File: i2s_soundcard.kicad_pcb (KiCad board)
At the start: 4 copper layers, 83.1 x 38.1 mm, 23 parts, among them J1 Conn_01x08, J2 Conn_01x06, J3 Conn_01x04, J4 Conn_01x11, J5 Conn_01x03, U1 TLV320AIC3104IRHBT, U2 TPA2006D1DRBR, U3 TPA2006D1DRBR, U6 TLV7111830DSER, U7 TPD4E02B04DQAR, U8 TPD4E02B04DQAR

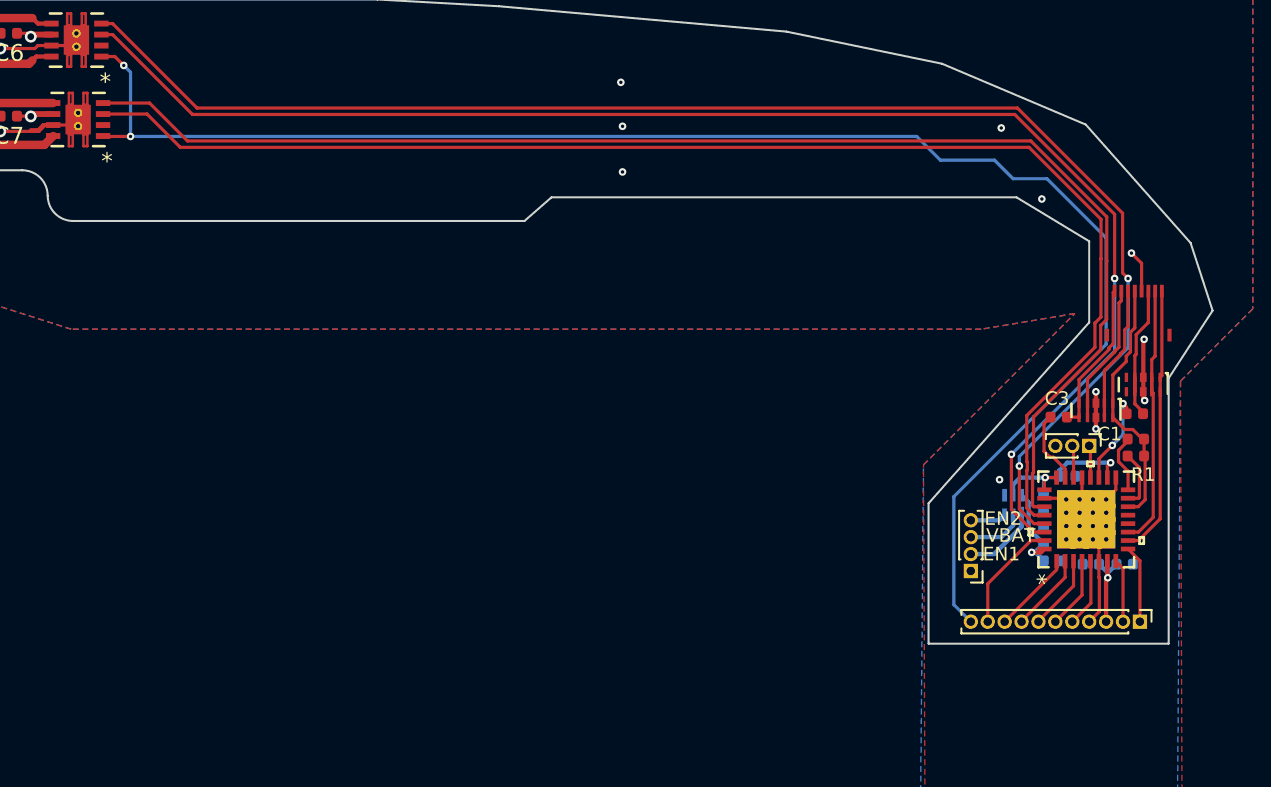
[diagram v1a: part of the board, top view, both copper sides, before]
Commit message: Change C2/C3 to 1206, adjust board to make that fit. Add courtyard to ESD protection diodes
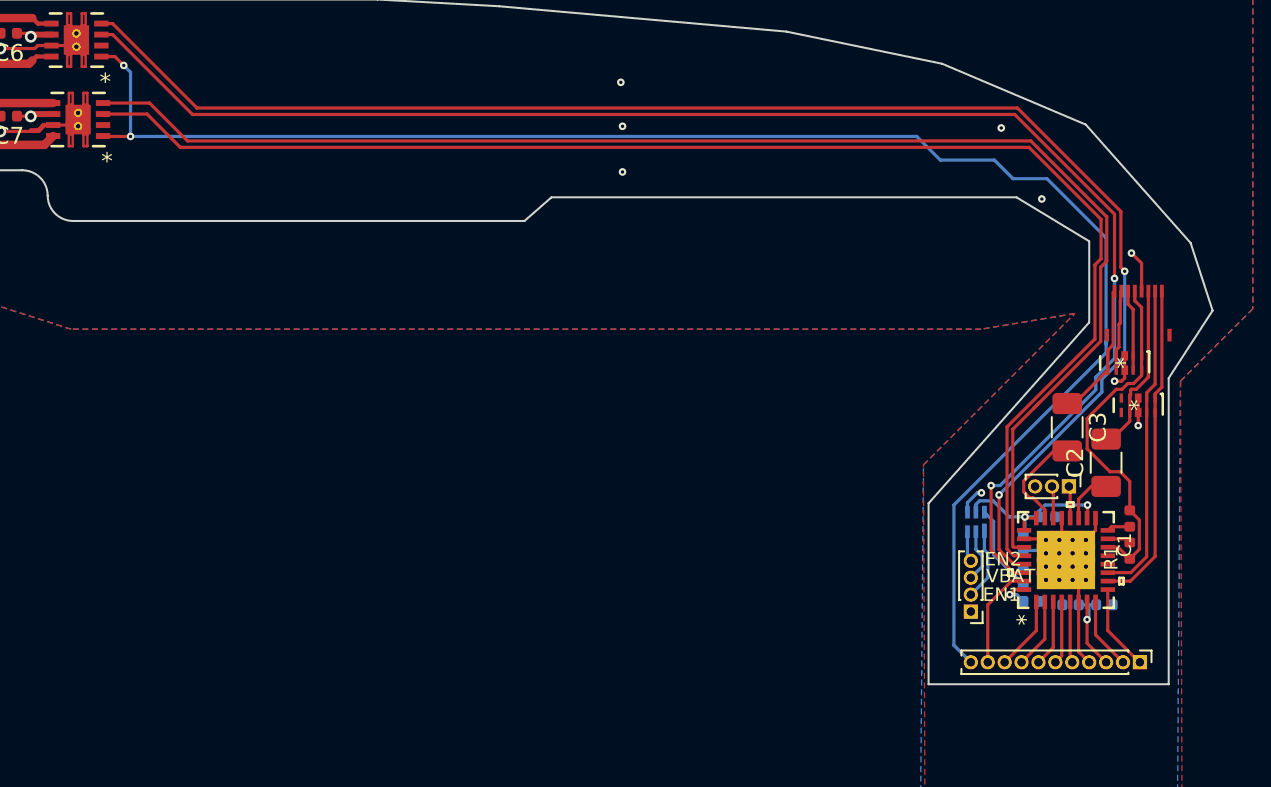
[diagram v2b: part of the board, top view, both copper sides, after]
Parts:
- C1: value C -> 100nF
- C2, C3: value C -> 220uF; footprint Capacitor_SMD:C_0402_1005Metric -> Capacitor_SMD:C_1206_3216Metric
- U7, U8: value TPD4E02B04DQAR -> DQA0010A
- moved R1 5.61 mm to (166.0, 90.9), turned to 90 degrees
- moved C1 4.71 mm to (166.0, 89.0), turned to 90 degrees
- moved C2 3.36 mm to (164.6, 85.7), turned to 90 degrees
- moved U8 3.28 mm to (165.7, 79.8)
- moved C4 2.68 mm to (159.7, 92.4)
- moved C5 2.68 mm to (159.7, 90.4)
- moved C8 2.68 mm to (160.2, 93.9)
- moved C9 2.68 mm to (161.1, 88.9)
- moved U1 2.68 mm to (162.2, 91.5)
- moved C10 2.68 mm to (162.5, 94.1)
- moved C11 2.68 mm to (164.5, 94.1)
- moved J5 2.68 mm to (162.4, 87.1)
- moved U6 2.42 mm to (156.9, 89.2)
- moved J3 2.40 mm to (156.6, 94.5)
- moved J4 2.40 mm to (166.6, 97.5)
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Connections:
- U1 pad 12: (no net) -> Net-(U1-Pad12)
- U1 pad 13: (no net) -> Net-(U1-Pad13)
- U2 pad 2: (no net) -> Net-(U2-Pad2)
- U3 pad 2: (no net) -> Net-(U3-Pad2)
- U7 pad 5: (no net) -> Net-(U7-Pad5)
- U7 pad 6: (no net) -> Net-(U7-Pad6)
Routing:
- net GND: track 36.5 -> 29.8 mm, vias 15 -> 13
- net /SLEEVE: track 15.2 -> 21.2 mm
- net /DETECT?: track 8.30 -> 4.80 mm
- net /spkr_amp_left/LINEIN+: track 81.8 -> 85.1 mm
- net /INTMIC_P: track 15.9 -> 19.3 mm
- net /RING2_AGAIN: track 8.05 -> 4.80 mm
- net /spkr_amp_right/LINEIN-: track 86.8 -> 90.0 mm
- net /spkr_amp_left/LINEIN-: track 81.7 -> 84.6 mm
- net /spkr_amp_right/LINEIN+: track 87.1 -> 89.9 mm
- net Net-(C2-Pad1): track 5.75 -> 3.06 mm, vias 2 -> 0
- net /~SHUTDOWN: track 94.5 -> 97.1 mm
- net /INTMIC_N: track 16.2 -> 18.6 mm
- net Net-(C1-Pad1): track 3.46 -> 1.39 mm
- net Net-(R1-Pad2): track 3.43 -> 1.39 mm
- net Net-(C3-Pad2): track 4.37 -> 6.13 mm
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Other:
- board size 83.1 x 38.1 mm -> 83.1 x 40.5 mm

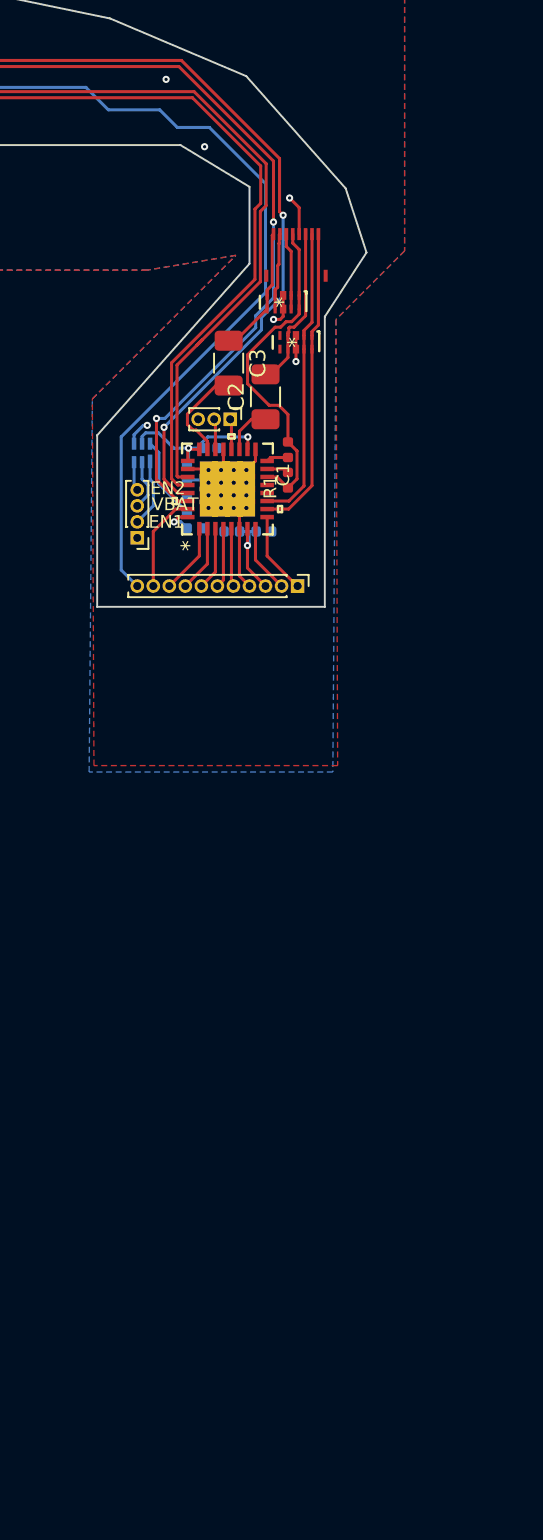
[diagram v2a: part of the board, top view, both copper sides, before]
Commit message: lay out new version with AIC3206 codec
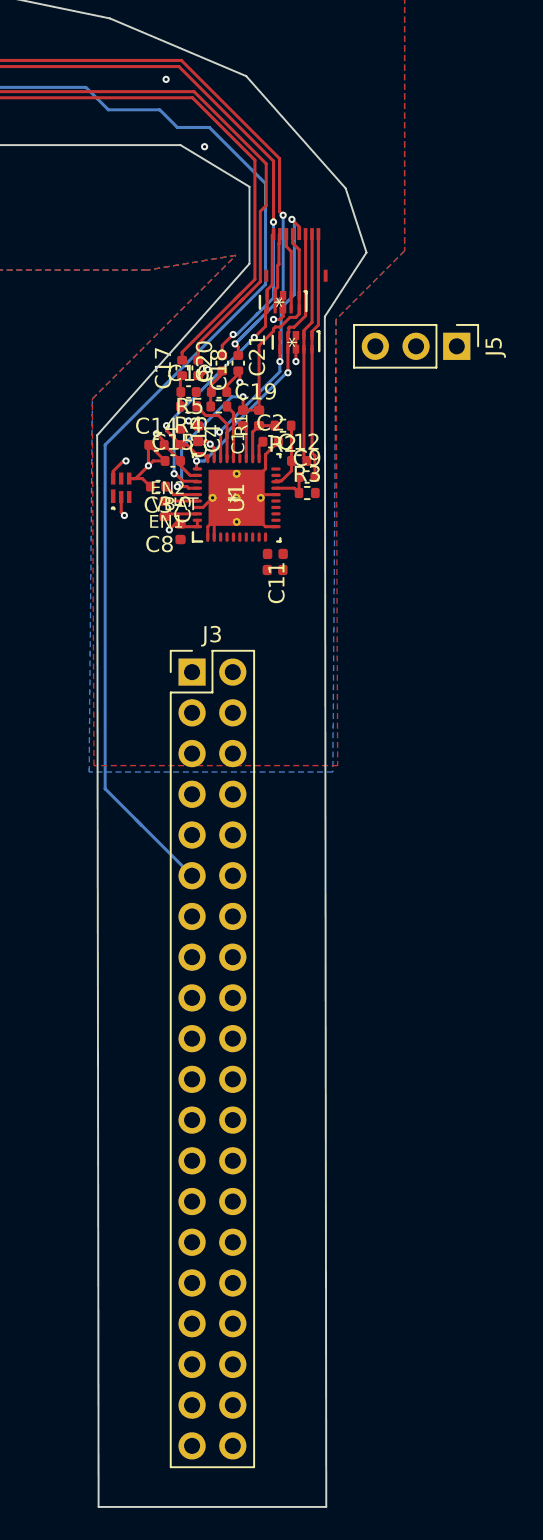
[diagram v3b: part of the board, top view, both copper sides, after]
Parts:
- removed J4: Conn_01x11, Connector_PinHeader_1.00mm:PinHeader_1x11_P1.00mm_Vertical
- added C12: 0.1u, Capacitor_SMD:C_0402_1005Metric, F.Cu at (166.7, 89.7)
- added C13: 10uF, Capacitor_SMD:C_0402_1005Metric, F.Cu at (159.3, 88.2)
- added C14: 10uF, Capacitor_SMD:C_0402_1005Metric, F.Cu at (157.8, 88.7)
- added C15: 0.1uF, Capacitor_SMD:C_0402_1005Metric, F.Cu at (158.8, 89.7)
- added C16: 4.7nF, Capacitor_SMD:C_0402_1005Metric, F.Cu at (159.8, 85.4)
- added C17: 0.1uF, Capacitor_SMD:C_0402_1005Metric, F.Cu at (159.4, 83.9)
- added C18: 0.1uF, Capacitor_SMD:C_0402_1005Metric, F.Cu at (160.4, 83.9)
- added C19: 4.7nF, Capacitor_SMD:C_0402_1005Metric, F.Cu at (161.7, 85.4)
- added C20: 0.1uF, Capacitor_SMD:C_0402_1005Metric, F.Cu at (161.9, 83.6)
- added C21: 0.1uF, Capacitor_SMD:C_0402_1005Metric, F.Cu at (162.9, 83.6)
- added R2: 1k, Resistor_SMD:R_0402_1005Metric, F.Cu at (165.7, 87.5)
- added R3: 1k, Resistor_SMD:R_0402_1005Metric, F.Cu at (167.2, 91.7)
- added R4: 1k, Resistor_SMD:R_0402_1005Metric, F.Cu at (159.8, 86.3)
- added R5: 1k, Resistor_SMD:R_0402_1005Metric, F.Cu at (161.7, 86.3)
- C10, C11, C4, C8, U6: moved to F.Cu
- C2: value 220uF -> 1uF; footprint Capacitor_SMD:C_1206_3216Metric -> Capacitor_SMD:C_0402_1005Metric
- C3: value 220uF -> 2.2uF; footprint Capacitor_SMD:C_1206_3216Metric -> Capacitor_SMD:C_0402_1005Metric
- C5: value 22uF -> 2.2uF; moved to F.Cu
- C9: value 220nF -> 0.1u; moved to F.Cu
- J3: value Conn_01x04 -> Conn_02x20_Odd_Even; footprint Connector_PinHeader_1.00mm:PinHeader_1x04_P1.00mm_Vertical -> Connector_PinHeader_2.54mm:PinHeader_2x20_P2.54mm_Vertical
- J5: footprint Connector_PinHeader_1.00mm:PinHeader_1x03_P1.00mm_Vertical -> Connector_PinHeader_2.54mm:PinHeader_1x03_P2.54mm_Vertical
- R1: value 2.2k -> 2.7k
- U1: value TLV320AIC3104IRHBT -> TLV320AIC3206IRSBR; footprint footprints:TLV320AIC3104IRHBT -> footprints:TLV320AIC3206IRSBR
- U7, U8: value DQA0010A -> TPD4E02B04DQAR
- moved J5 14.8 mm to (176.5, 82.5)
- moved J3 9.04 mm to (160.0, 102.9), turned to 0 degrees
- moved C3 8.87 mm to (157.9, 91.3), turned to 180 degrees
- moved C9 6.36 mm to (167.2, 90.7)
- moved C4 4.46 mm to (160.4, 88.0)
- moved R1 4.28 mm to (164.2, 87.0)
- moved C10 3.61 mm to (165.2, 96.5), turned to 180 degrees
- moved C1 3.43 mm to (163.2, 87.0)
- moved C2 2.82 mm to (164.9, 88.5), turned to 0 degrees
- moved C5 2.69 mm to (158.3, 92.7)
- moved U6 2.53 mm to (155.6, 91.4)
- moved C11 1.57 mm to (165.2, 95.5)
- moved C8 0.93 mm to (159.3, 94.1), turned to 90 degrees
- moved U1 0.80 mm to (162.8, 92.0)
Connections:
- C2 pad 2: /TIP -> GND
- C3 pad 1: /RING1 -> Net-(C3-Pad1)
- C3 pad 2: Net-(C3-Pad2) -> GND
- C5 pad 1: /VCC3.0 -> Net-(C5-Pad1)
- C5 pad 2: GND -> Net-(C5-Pad2)
- C6 pad 1: /VBAT_3.7 -> /VSYS
- C7 pad 1: /VBAT_3.7 -> /VSYS
- C9 pad 1: /VCC3.0 -> Net-(C9-Pad1)
- C9 pad 2: GND -> /INTMIC_P
- J1 pad 4: GND -> /RING2
- J3 pad 1: GND -> /IOVDD
- J3 pad 2: /EN1 -> /VSYS
- J3 pad 3: /VBAT_3.7 -> /SDA
- J3 pad 4: /EN2 -> /VSYS
- R1 pad 1: /SLEEVE -> Net-(R1-Pad1)
- R1 pad 2: Net-(R1-Pad2) -> /SLEEVE
- U1 pad 1: /MCLK -> GND
- U1 pad 10: /INTMIC_P -> /IOVDD
- U1 pad 11: /INTMIC_N -> GND
- U1 pad 12: Net-(U1-Pad12) -> unconnected-(U1-Pad12)
- U1 pad 13: Net-(U1-Pad13) -> /SCL
- U1 pad 14: /SLEEVE -> /SDA
- U1 pad 15: Net-(R1-Pad2) -> unconnected-(U1-Pad15)
- U1 pad 16: Net-(C1-Pad1) -> GND
- U1 pad 17: GND -> Net-(C9-Pad1)
- U1 pad 18: /VCC3.0 -> Net-(C12-Pad1)
- U1 pad 19: Net-(C2-Pad1) -> unconnected-(U1-Pad19)
- U1 pad 2: /BCLK -> GND
- U1 pad 20: /LOL -> unconnected-(U1-Pad20)
- U1 pad 22: /LOR -> Net-(C2-Pad1)
- U1 pad 23: Net-(C3-Pad2) -> Net-(R1-Pad1)
- U1 pad 24: /VCC3.0 -> Net-(C1-Pad1)
- U1 pad 25: /VCC3.0 -> unconnected-(U1-Pad25)
- U1 pad 26: GND -> /LOL
- U1 pad 27: /spkr_amp_left/LINEIN+ -> /LOR
- U1 pad 28: /spkr_amp_left/LINEIN- -> /RING2
- U1 pad 29: /spkr_amp_right/LINEIN+ -> /VCC1.8
- U1 pad 3: /WCLK -> /CODEC_RESET
- U1 pad 30: /spkr_amp_right/LINEIN- -> /VSYS
- U1 pad 31: /RESET -> /TIP
- U1 pad 33: GND -> /RING1
- U1 pad 4: /DIN -> unconnected-(U1-Pad4)
- U1 pad 5: /DOUT -> /MCLK
- U1 pad 6: GND -> /BCLK
- U1 pad 7: /IOVDD -> /WCLK
- U1 pad 8: /SCL -> /DIN
- U1 pad 9: /SCA -> /DOUT
- U2 pad 1: /~SHUTDOWN -> /~AMP_SHUTDOWN
- U2 pad 2: Net-(U2-Pad2) -> unconnected-(U2-Pad2)
- U2 pad 3: /spkr_amp_left/LINEIN- -> Net-(C17-Pad2)
- U2 pad 4: /spkr_amp_left/LINEIN+ -> Net-(C18-Pad2)
- U2 pad 6: /VBAT_3.7 -> /VSYS
- U3 pad 1: /~SHUTDOWN -> /~AMP_SHUTDOWN
- U3 pad 2: Net-(U3-Pad2) -> unconnected-(U3-Pad2)
- U3 pad 3: /spkr_amp_right/LINEIN- -> Net-(C20-Pad2)
- U3 pad 4: /spkr_amp_right/LINEIN+ -> Net-(C21-Pad2)
- U3 pad 6: /VBAT_3.7 -> /VSYS
- U6 pad 1: /EN1 -> /LDO_EN1
- U6 pad 2: /VBAT_3.7 -> /VSYS
- U6 pad 3: /EN2 -> unconnected-(U6-Pad3)
- U6 pad 5: /VCC3.0 -> unconnected-(U6-Pad5)
- U7 pad 5: Net-(U7-Pad5) -> /RING2
- U7 pad 6: Net-(U7-Pad6) -> /RING2
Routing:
- net /~AMP_SHUTDOWN: track 0.00 -> 117.8 mm, vias 0 -> 2
- net /~SHUTDOWN: track 97.1 -> 0.00 mm, vias 2 -> 0
- net /spkr_amp_right/LINEIN-: track 90.0 -> 0.00 mm, vias 2 -> 0
- net /spkr_amp_right/LINEIN+: track 89.9 -> 0.00 mm, vias 2 -> 0
- net /spkr_amp_left/LINEIN+: track 85.1 -> 0.00 mm
- net /spkr_amp_left/LINEIN-: track 84.6 -> 0.00 mm
- net Net-(C21-Pad2): track 0.00 -> 80.6 mm, vias 0 -> 2
- net Net-(C20-Pad2): track 0.00 -> 78.0 mm, vias 0 -> 2
- net Net-(C18-Pad2): track 0.00 -> 76.5 mm
- net Net-(C17-Pad2): track 0.00 -> 75.9 mm
- net /RING2: track 0.00 -> 19.7 mm, vias 0 -> 3
- net GND: track 29.8 -> 42.9 mm, vias 13 -> 15
- net /RING1: track 7.63 -> 19.2 mm, vias 0 -> 2
- net /VCC3.0: track 11.4 -> 0.00 mm, vias 2 -> 0
- net /VSYS: track 0.00 -> 9.26 mm, vias 0 -> 4
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- added copper zone on In2.Cu, net /VCC1.8
- added copper zone on In2.Cu, net /VSYS
- removed copper zone on In2.Cu, net /VBAT_3.7
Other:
- board size 83.1 x 40.5 mm -> 83.1 x 96.6 mm
- net class Default removed
- net class Power removed
- rule pad_to_mask_clearance: 0.05 -> 0

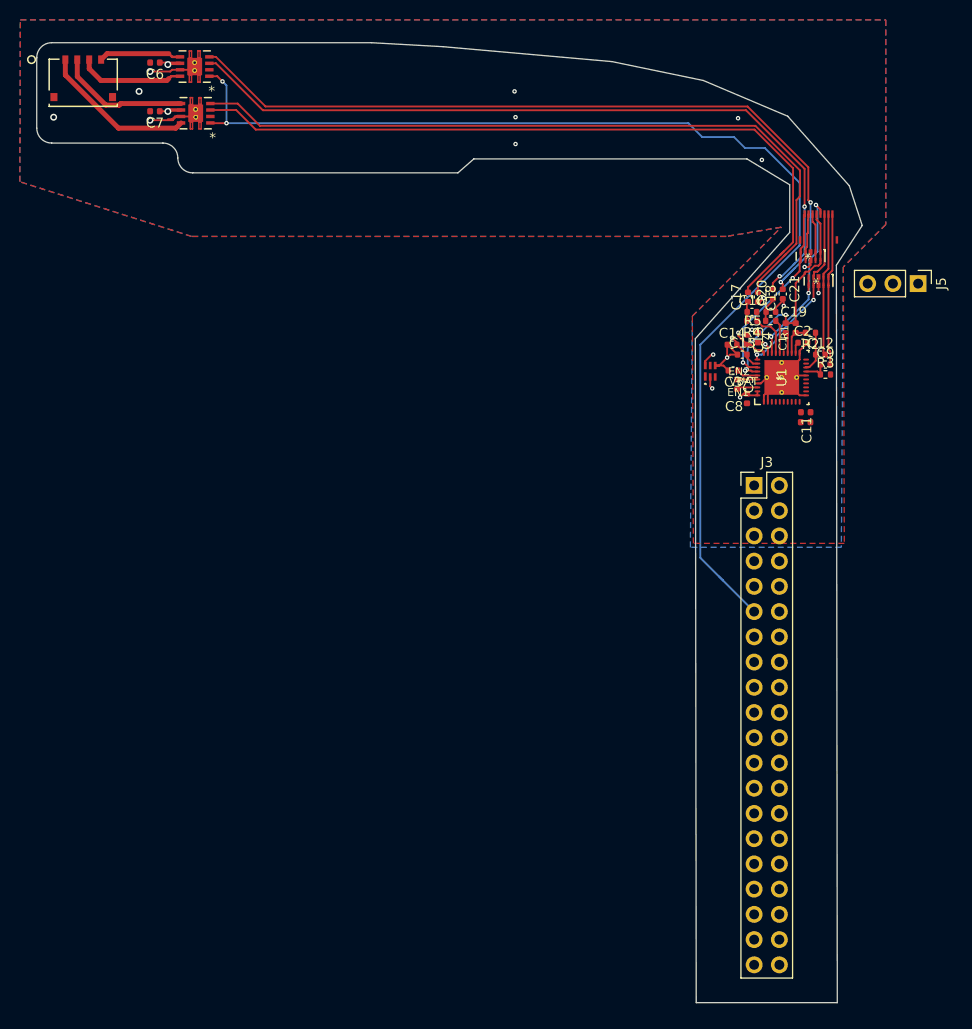
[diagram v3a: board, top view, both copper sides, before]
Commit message: Add an audio switch back in. Finish layout.
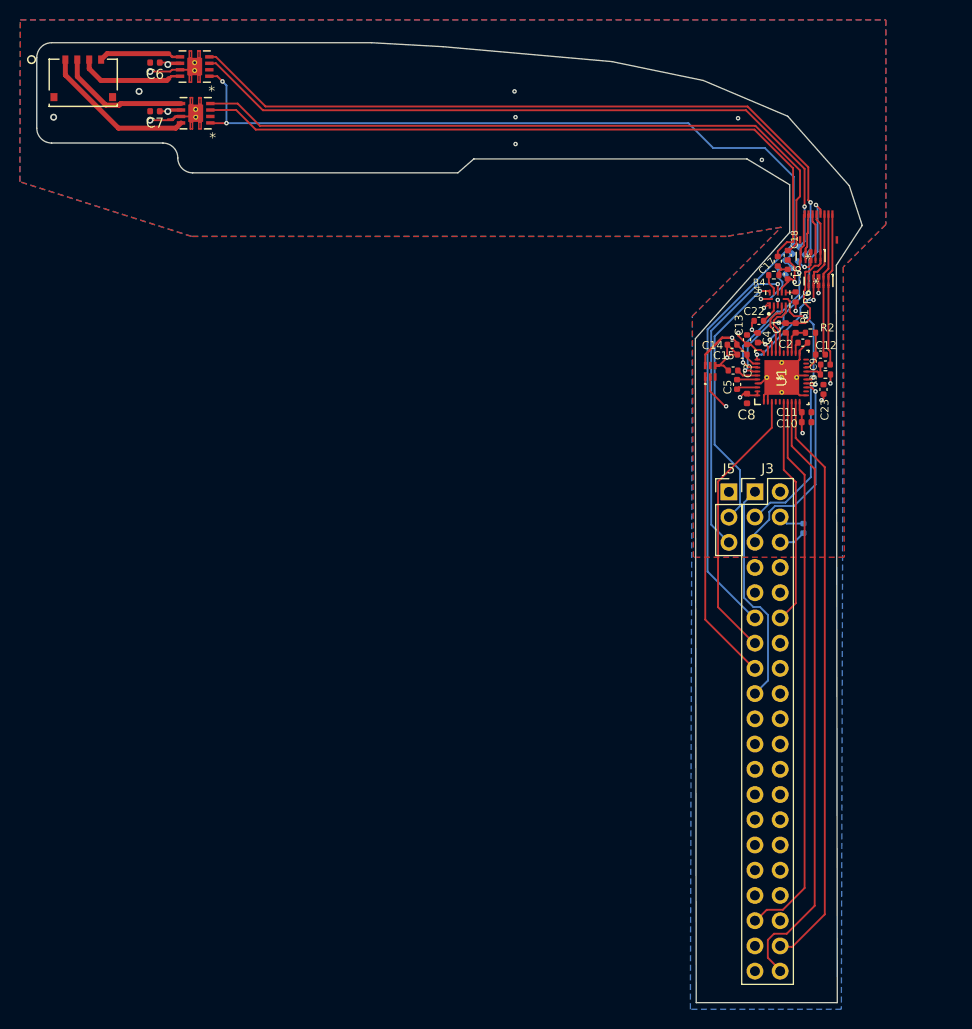
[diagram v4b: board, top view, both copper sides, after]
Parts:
- added C22: 0.1uF, Capacitor_SMD:C_0402_1005Metric, F.Cu at (160.5, 86.3)
- added C23: 10uF, Capacitor_SMD:C_0402_1005Metric, F.Cu at (167.0, 93.2)
- added C24: 10uF, Capacitor_SMD:C_0402_1005Metric, B.Cu at (165.0, 107.2)
- added R6: R, Resistor_SMD:R_0402_1005Metric, F.Cu at (164.2, 83.9)
- added U4: FSA2275UMX, footprints:FSA2275, F.Cu at (162.4, 84.1)
- C19, C20, C21, R5: moved to B.Cu
- moved J5 28.3 mm to (157.5, 103.5), turned to 0 degrees
- moved R5 5.81 mm to (162.8, 80.6), turned to 45 degrees
- moved C16 5.23 mm to (163.4, 81.6), turned to -90 degrees
- moved C18 5.16 mm to (163.4, 79.7)
- moved R4 5.10 mm to (162.0, 81.7), turned to 0 degrees
- moved C20 4.96 mm to (164.2, 79.2), turned to 45 degrees
- moved C17 4.69 mm to (162.4, 80.3)
- moved C19 4.48 mm to (163.5, 81.3), turned to -135 degrees
- moved C21 4.07 mm to (164.8, 80.0), turned to 45 degrees
- moved J3 0.64 mm to (160.1, 103.5)
- moved C10 0.10 mm to (165.3, 96.5)
- moved C11 0.09 mm to (165.3, 95.5)
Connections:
- J5 pad 1: /LOL -> GND
- J5 pad 3: GND -> /LOL
- R4 pad 1: /LOR -> /SPKR_R
- R5 pad 1: /LOL -> /SPKR_L
- U1 pad 15: unconnected-(U1-Pad15) -> /SPKR_LO_SEL
- U1 pad 26: /LOL -> /CODEC_LOL
- U1 pad 27: /LOR -> /CODEC_LOR
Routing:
- net /DIN: track 0.00 -> 61.7 mm
- net /DOUT: track 0.00 -> 58.7 mm
- net /WCLK: track 0.00 -> 56.1 mm
- net /IOVDD: track 0.00 -> 33.9 mm, vias 0 -> 1
- net /LDO_EN1: track 0.00 -> 31.6 mm
- net /CODEC_RESET: track 0.00 -> 28.2 mm
- net /LOL: track 3.42 -> 31.5 mm, vias 0 -> 1
- net /BCLK: track 0.00 -> 23.0 mm
- net /LOR: track 4.50 -> 27.2 mm, vias 0 -> 1
- net /SCL: track 0.00 -> 20.0 mm, vias 0 -> 1
- net /SDA: track 0.00 -> 17.9 mm, vias 0 -> 1
- net /SPKR_LO_SEL: track 0.00 -> 10.7 mm, vias 0 -> 2
- net GND: track 42.9 -> 51.9 mm, vias 15 -> 17
- net Net-(C21-Pad2): track 80.6 -> 74.0 mm, vias 2 -> 1
- net /VSYS: track 9.26 -> 15.7 mm, vias 4 -> 6
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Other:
- board text removed: "BCLK"
- board text removed: "DIN"
- board text removed: "DO"
- board text removed: "EN1"
- board text removed: "EN2"
- board text removed: "GND"
- board text removed: "IOVDD"
- board text removed: "MCLK"
- board text removed: "RST"
- board text removed: "SCL"
- board text removed: "SDA"
- board text removed: "VBAT"
- board text removed: "WCLK"
- board text removed: "~SD"
